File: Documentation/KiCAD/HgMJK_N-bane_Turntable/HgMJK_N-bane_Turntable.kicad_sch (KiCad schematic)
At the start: 7 parts, among them M1 Stepper_Motor_unipolar_5pin, U1 ULN2003

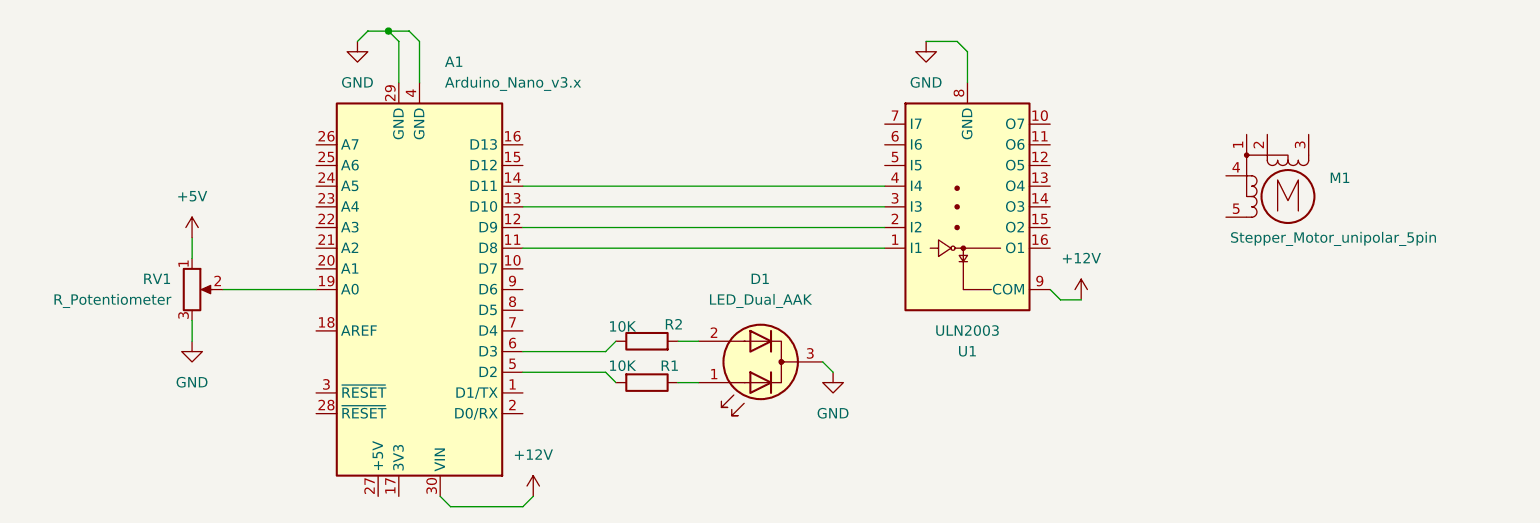
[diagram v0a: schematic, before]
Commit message: edit code and file name
edit *.ino filename. Edit/updated code for only Uno/Nano and Mega2560 MCU board
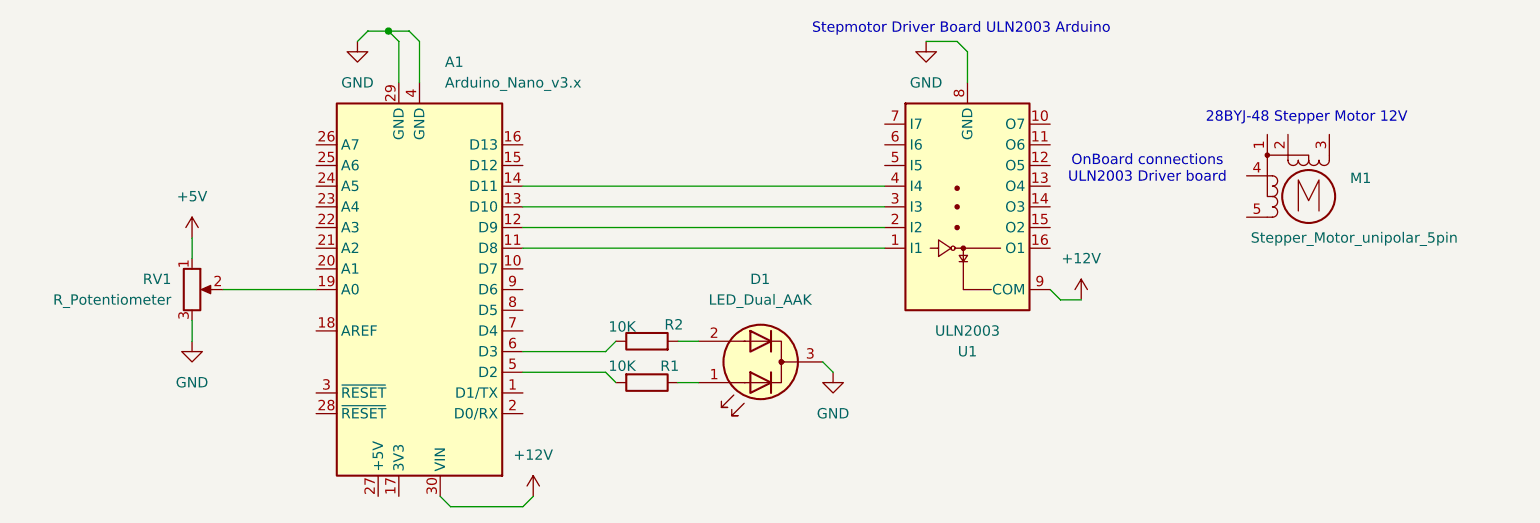
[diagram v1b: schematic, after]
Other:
- note added: "28BYJ-48 Stepper Motor 12V"
- note added: "OnBoard connections ULN2003 Driver board"
- note added: "Stepmotor Driver Board ULN2003 Arduino"
- company: (none) -> EaCode
- title: (none) -> Pot-meter controller for stepMotor
- moved on the sheet: M1
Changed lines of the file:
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@@
 	(generator_version "9.0")
 	(paper "A4")
+	(title_block
+		(title "Pot-meter controller for stepMotor")
+		(date "2025-04-02")
+		(rev "ver. 0.1")
+		(company "EaCode")
+		(comment 1 "HgMJK, N.bane")
+	)
+	(text "OnBoard connections\nULN2003 Driver board"
+		(exclude_from_sim no)
+		(at 168.148 62.738 0)
+		(effects
+			(font
+				(size 1.27 1.27)
+			)
+		)
+	)
+	(text "28BYJ-48 Stepper Motor 12V"
+		(exclude_from_sim no)
+		(at 187.706 56.388 0)
+		(effects
+			(font
+				(size 1.27 1.27)
+			)
+		)
+	)
+	(text "Stepmotor Driver Board ULN2003 Arduino"
+		(exclude_from_sim no)
+		(at 145.288 45.466 0)
+		(effects
+			(font
+				(size 1.27 1.27)
+			)
+		)
+	)
 	(junction
 		(at 74.93 45.72)
@@
 	(symbol
 		(lib_id "Motor:Stepper_Motor_unipolar_5pin")
-		(at 185.42 66.04 0)
+		(at 187.96 66.04 0)
 		(unit 1)
 		(exclude_from_sim no)
@@
 		(dnp no)
 		(property "Reference" "M1"
-			(at 190.5 63.792 0)
+			(at 193.04 63.792 0)
 			(effects
 				(font
@@
 		)
 		(property "Value" "Stepper_Motor_unipolar_5pin"
-			(at 178.308 71.12 0)
+			(at 180.848 71.12 0)
 			(effects
 				(font
@@
 		)
 		(property "Footprint" ""
-			(at 185.674 66.294 0)
+			(at 188.214 66.294 0)
 			(effects
 				(font
@@
 		)
 		(property "Datasheet" "http://www.infineon.com/dgdl/Application-Note-TLE8110EE_driving_UniPolarStepperMotor_V1.1.pdf?fileId=db3a30431be39b97011be5d0aa0a00b0"
-			(at 185.674 66.294 0)
+			(at 188.214 66.294 0)
 			(effects
 				(font
@@
 		)
 		(property "Description" "5-wire unipolar stepper motor"
-			(at 185.42 66.04 0)
-			(effects
-				(font
+			(at 187.96 66.04 0)
+			(effects
+				(font
